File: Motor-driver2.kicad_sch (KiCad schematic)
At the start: 32 parts, among them J12 PINHD_1x4_Male, J15 PINHD_1x4_Male, U4 DRV8825PWP, U5 DRV8825PWP

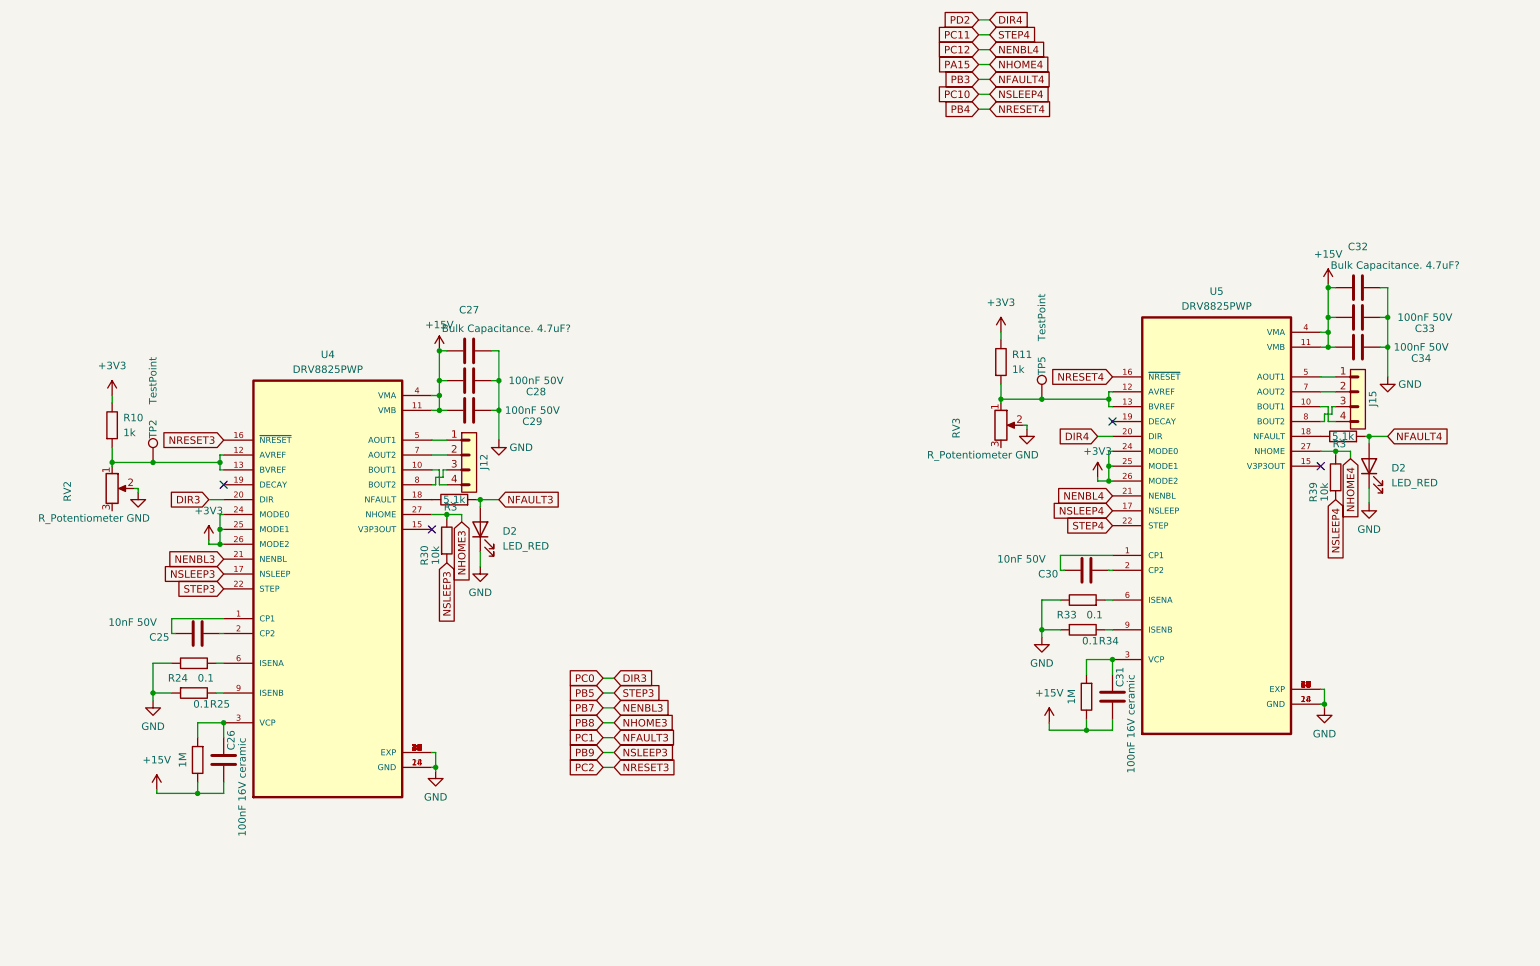
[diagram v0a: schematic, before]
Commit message: completly reroutet EVERYTHING
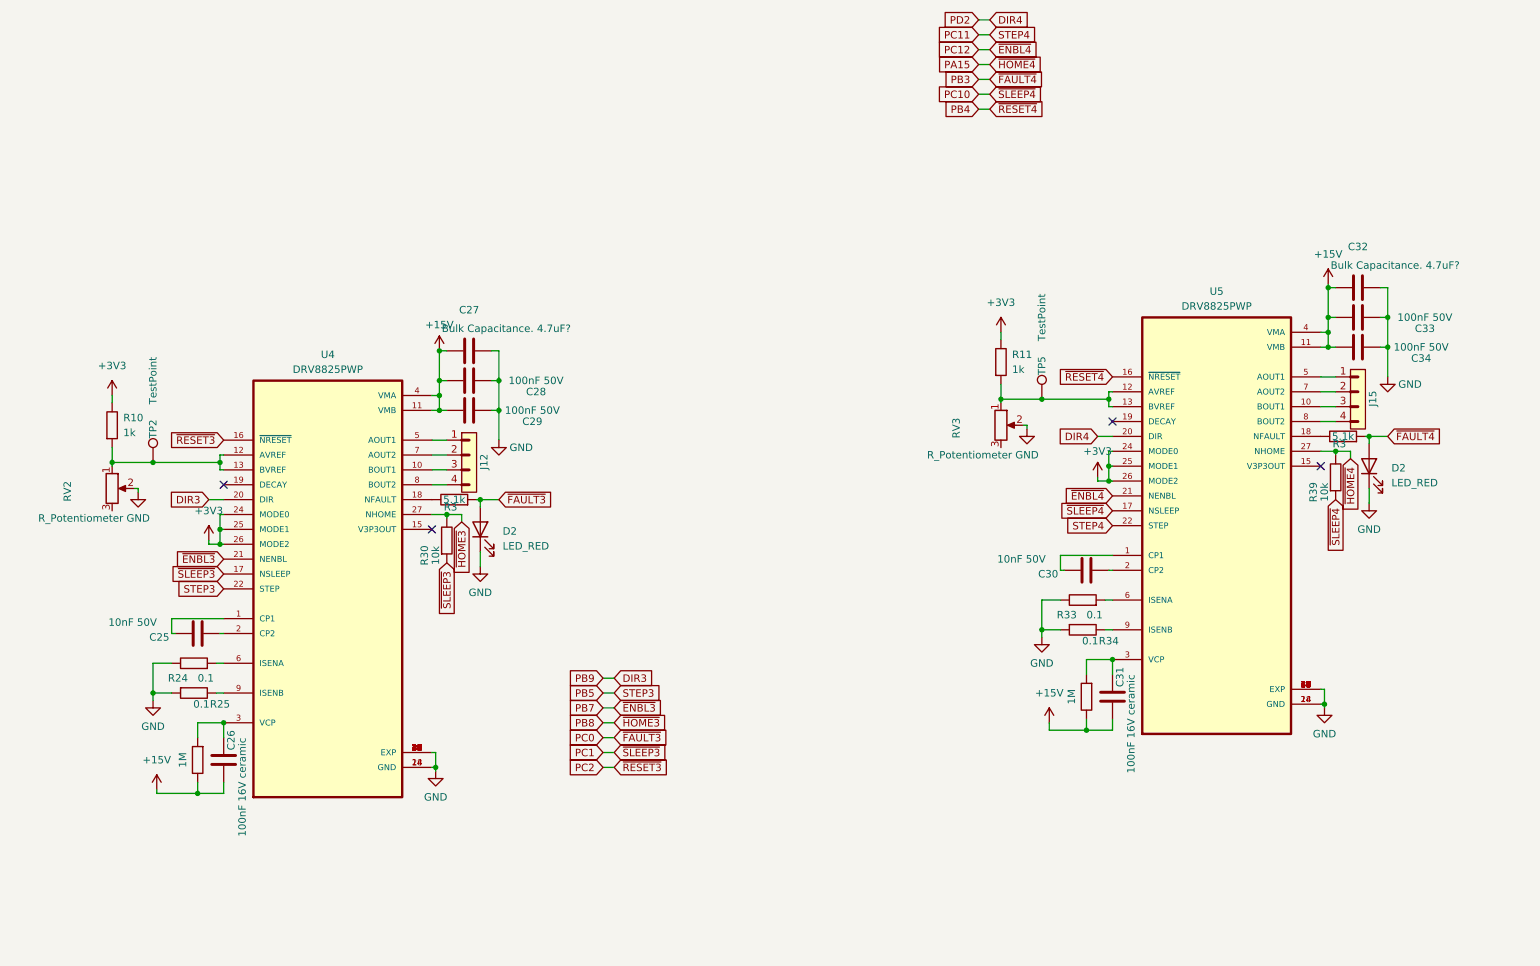
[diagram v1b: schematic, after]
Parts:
- RV2, RV3: footprint Potentiometer_THT:Potentiometer_ACP_CA6-H2,5_Horizontal -> poti:3386P1473LF
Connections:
- net at J15.3: now also U5.10 (BOUT1); no longer U5.8 (BOUT2)
- net at J15.4: now also U5.8 (BOUT2); no longer U5.10 (BOUT1)
- net at U4.10 (BOUT1): now also J12.3; no longer J12.4
- net at U4.8 (BOUT2): now also J12.4; no longer J12.3
- net NENBL3 renamed PB7
- net NENBL4 renamed PC12
- net NFAULT3 renamed PC0
- net NFAULT4 renamed PB3
- net NHOME3 renamed PB8
- net NHOME4 renamed PA15
- net NRESET3 renamed PC2
- net NRESET4 renamed PB4
- net NSLEEP3 renamed PC1
- net NSLEEP4 renamed PC10

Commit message: deTommaso approved version
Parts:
- removed C27, C32: Bulk Capacitance. 4.7uF?, Capacitor_SMD:C_0805_2012Metric, symbol Device:C
- removed TP2, TP5: TestPoint, TestPoint:TestPoint_Pad_D1.5mm, symbol Connector:TestPoint
- added C22 (x2): 10uF, Capacitor_THT:C_Radial_D5.0mm_H5.0mm_P2.00mm, symbol Device:C
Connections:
- net +15V: now also C22.2, C22.2
- net GND: now also C22.1, C22.1
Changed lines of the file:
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@@
   (junction (at 51.435 102.235) (diameter 0) (color 0 0 0 0)
   )
-  (junction (at 40.005 102.235) (diameter 0) (color 0 0 0 0)
-  )
   (junction (at 52.07 146.685) (diameter 0) (color 0 0 0 0)
   )
@@
   )
   (junction (at 184.785 91.44) (diameter 0) (color 0 0 0 0)
-  )
-  (junction (at 191.77 91.44) (diameter 0) (color 0 0 0 0)
   )
   (junction (at 199.39 147.955) (diameter 0) (color 0 0 0 0)
@@
     (stroke (width 0) (type default))
   )
-  (wire (pts (xy 33.02 102.235) (xy 40.005 102.235))
+  (wire (pts (xy 33.02 102.235) (xy 51.435 102.235))
     (stroke (width 0) (type default))
   )
@@
     (stroke (width 0) (type default))
   )
-  (wire (pts (xy 191.77 91.44) (xy 203.2 91.44))
+  (wire (pts (xy 184.785 91.44) (xy 203.2 91.44))
     (stroke (width 0) (type default))
   )
@@
     (stroke (width 0) (type default))
   )
-  (wire (pts (xy 40.005 102.235) (xy 51.435 102.235))
-    (stroke (width 0) (type default))
-  )
   (wire (pts (xy 116.84 144.145) (xy 118.745 144.145))
     (stroke (width 0) (type default))
@@
   )
   (wire (pts (xy 199.39 147.955) (xy 203.835 147.955))
-    (stroke (width 0) (type default))
-  )
-  (wire (pts (xy 184.785 91.44) (xy 191.77 91.44))
     (stroke (width 0) (type default))
   )
@@
     )
   )
-  (symbol (lib_id "Device:C") (at 93.98 83.185 270) (unit 1)
-    (in_bom yes) (on_board yes) (dnp no)
-    (property "Reference" "C27" (at 93.98 76.2 90)
-      (effects (font (size 1.27 1.27)))
-    )
-    (property "Value" "Bulk Capacitance. 4.7uF?" (at 100.33 79.375 90)
-      (effects (font (size 1.27 1.27)))
-    )
-    (property "Footprint" "Capacitor_SMD:C_0805_2012Metric" (at 90.17 84.1502 0)
-      (effects (font (size 1.27 1.27)) hide)
-    )
-    (property "Datasheet" "~" (at 93.98 83.185 0)
-      (effects (font (size 1.27 1.27)) hide)
-    )
-    (pin "1")
-    (pin "2")
-    (instances
-      (project "Doodle Drive"
-        (path "/3ec634aa-8c09-482d-9325-2288a4dbd68b/4a4951fa-be57-4d48-97a5-6be750b353b5"
-          (reference "C27") (unit 1)
+  (symbol (lib_id "Device:C") (at 245.745 72.39 270) (unit 1)
+    (in_bom yes) (on_board yes) (dnp no)
+    (property "Reference" "C22" (at 245.745 65.405 90)
+      (effects (font (size 1.27 1.27)))
+    )
+    (property "Value" "10uF" (at 246.38 68.58 90)
+      (effects (font (size 1.27 1.27)))
+    )
+    (property "Footprint" "Capacitor_THT:C_Radial_D5.0mm_H5.0mm_P2.00mm" (at 241.935 73.3552 0)
+      (effects (font (size 1.27 1.27)) hide)
+    )
+    (property "Datasheet" "~" (at 245.745 72.39 0)
+      (effects (font (size 1.27 1.27)) hide)
+    )
+    (pin "1")
+    (pin "2")
+    (instances
+      (project "Doodle Drive"
+        (path "/3ec634aa-8c09-482d-9325-2288a4dbd68b/ce40ab82-c304-4dd2-80f5-b6df1964b151"
+          (reference "C22") (unit 1)
+        )
+        (path "/3ec634aa-8c09-482d-9325-2288a4dbd68b/bef0954e-6024-4756-b9a6-5ea2a0825f13"
+          (reference "C37") (unit 1)
+        )
+        (path "/3ec634aa-8c09-482d-9325-2288a4dbd68b/4a4951fa-be57-4d48-97a5-6be750b353b5"
+          (reference "C32") (unit 1)
         )
       )
@@
   )
   (symbol (lib_id "power:+15V") (at 88.9 83.185 0) (unit 1)
-    (in_bom yes) (on_board yes) (dnp no) (fields_autoplaced)
+    (in_bom yes) (on_board yes) (dnp no)
     (property "Reference" "#PWR066" (at 88.9 86.995 0)
       (effects (font (size 1.27 1.27)) hide)
     )
-    (property "Value" "+15V" (at 88.9 78.74 0)
+    (property "Value" "+15V" (at 85.09 81.28 0)
       (effects (font (size 1.27 1.27)))
     )
@@
         (path "/3ec634aa-8c09-482d-9325-2288a4dbd68b/4a4951fa-be57-4d48-97a5-6be750b353b5"
           (reference "#PWR054") (unit 1)
-        )
-      )
-    )
-  )
-  (symbol (lib_id "Connector:TestPoint") (at 40.005 102.235 0) (unit 1)
-    (in_bom yes) (on_board yes) (dnp no)
-    (property "Reference" "TP2" (at 40.005 96.52 90)
-      (effects (font (size 1.27 1.27)))
-    )
-    (property "Value" "TestPoint" (at 40.005 88.265 90)
-      (effects (font (size 1.27 1.27)))
-    )
-    (property "Footprint" "TestPoint:TestPoint_Pad_D1.5mm" (at 45.085 102.235 0)
-      (effects (font (size 1.27 1.27)) hide)
-    )
-    (property "Datasheet" "~" (at 45.085 102.235 0)
-      (effects (font (size 1.27 1.27)) hide)
-    )
-    (pin "1")
-    (instances
-      (project "Doodle Drive"
-        (path "/3ec634aa-8c09-482d-9325-2288a4dbd68b/4a4951fa-be57-4d48-97a5-6be750b353b5"
-          (reference "TP2") (unit 1)
-        )
-        (path "/3ec634aa-8c09-482d-9325-2288a4dbd68b/ce40ab82-c304-4dd2-80f5-b6df1964b151"
-          (reference "TP42") (unit 1)
         )
       )
@@
     )
   )
-  (symbol (lib_id "Device:C") (at 245.745 72.39 270) (unit 1)
-    (in_bom yes) (on_board yes) (dnp no)
-    (property "Reference" "C32" (at 245.745 65.405 90)
-      (effects (font (size 1.27 1.27)))
-    )
-    (property "Value" "Bulk Capacitance. 4.7uF?" (at 252.095 68.58 90)
-      (effects (font (size 1.27 1.27)))
-    )
-    (property "Footprint" "Capacitor_SMD:C_0805_2012Metric" (at 241.935 73.3552 0)
-      (effects (font (size 1.27 1.27)) hide)
-    )
-    (property "Datasheet" "~" (at 245.745 72.39 0)
-      (effects (font (size 1.27 1.27)) hide)
-    )
-    (pin "1")
-    (pin "2")
-    (instances
-      (project "Doodle Drive"
-        (path "/3ec634aa-8c09-482d-9325-2288a4dbd68b/4a4951fa-be57-4d48-97a5-6be750b353b5"
-          (reference "C32") (unit 1)
-        )
-      )
-    )
-  )
   (symbol (lib_id "power:+3V3") (at 49.53 115.57 0) (unit 1)
     (in_bom yes) (on_board yes) (dnp no) (fields_autoplaced)
@@
         (path "/3ec634aa-8c09-482d-9325-2288a4dbd68b/4a4951fa-be57-4d48-97a5-6be750b353b5"
           (reference "C31") (unit 1)
-        )
-      )
-    )
-  )
-  (symbol (lib_id "Connector:TestPoint") (at 191.77 91.44 0) (unit 1)
-    (in_bom yes) (on_board yes) (dnp no)
-    (property "Reference" "TP5" (at 191.77 85.725 90)
-      (effects (font (size 1.27 1.27)))
-    )
-    (property "Value" "TestPoint" (at 191.77 77.47 90)
-      (effects (font (size 1.27 1.27)))
-    )
-    (property "Footprint" "TestPoint:TestPoint_Pad_D1.5mm" (at 196.85 91.44 0)
-      (effects (font (size 1.27 1.27)) hide)
-    )
-    (property "Datasheet" "~" (at 196.85 91.44 0)
-      (effects (font (size 1.27 1.27)) hide)
-    )
-    (pin "1")
-    (instances
-      (project "Doodle Drive"
-        (path "/3ec634aa-8c09-482d-9325-2288a4dbd68b/4a4951fa-be57-4d48-97a5-6be750b353b5"
-          (reference "TP5") (unit 1)
-        )
-        (path "/3ec634aa-8c09-482d-9325-2288a4dbd68b/ce40ab82-c304-4dd2-80f5-b6df1964b151"
-          (reference "TP42") (unit 1)
         )
       )
@@
         )
       )
+    )
+  )
+  (symbol (lib_id "Device:C") (at 93.98 83.185 270) (unit 1)
+    (in_bom yes) (on_board yes) (dnp no)
+    (property "Reference" "C22" (at 93.98 76.2 90)
+      (effects (font (size 1.27 1.27)))
+    )
+    (property "Value" "10uF" (at 94.615 79.375 90)
+      (effects (font (size 1.27 1.27)))
+    )
+    (property "Footprint" "Capacitor_THT:C_Radial_D5.0mm_H5.0mm_P2.00mm" (at 90.17 84.1502 0)
+      (effects (font (size 1.27 1.27)) hide)
+    )
+    (property "Datasheet" "~" (at 93.98 83.185 0)
+      (effects (font (size 1.27 1.27)) hide)
+    )
+    (pin "1")
+    (pin "2")
+    (instances
+      (project "Doodle Drive"
+        (path "/3ec634aa-8c09-482d-9325-2288a4dbd68b/ce40ab82-c304-4dd2-80f5-b6df1964b151"
+          (reference "C22") (unit 1)
+        )
+        (path "/3ec634aa-8c09-482d-9325-2288a4dbd68b/bef0954e-6024-4756-b9a6-5ea2a0825f13"
+          (reference "C37") (unit 1)
+        )
+        (path "/3ec634aa-8c09-482d-9325-2288a4dbd68b/4a4951fa-be57-4d48-97a5-6be750b353b5"
+          (reference "C27") (unit 1)
+        )
+      )

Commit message: bestellte version
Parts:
- C25, C30: value 10nF 50V -> 10nF
- C26, C31: value 100nF 16V ceramic -> 100nF
- C28, C29, C33, C34: value 100nF 50V -> 100nF
- R24, R25, R33, R34: footprint Resistor_SMD:R_0805_2012Metric -> Resistor_SMD:R_1206_3216Metric
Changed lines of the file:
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@@
       (effects (font (size 1.27 1.27)) (justify left))
     )
-    (property "Value" "10nF 50V" (at 184.15 118.745 90)
+    (property "Value" "10nF" (at 184.15 118.745 90)
       (effects (font (size 1.27 1.27)) (justify left))
     )
@@
       (effects (font (size 1.27 1.27)))
     )
-    (property "Value" "100nF 50V" (at 256.54 82.55 90)
+    (property "Value" "100nF" (at 256.54 82.55 90)
       (effects (font (size 1.27 1.27)))
     )
@@
       (effects (font (size 1.27 1.27)))
     )
-    (property "Value" "100nF 50V" (at 105.41 88.265 90)
+    (property "Value" "100nF" (at 105.41 88.265 90)
       (effects (font (size 1.27 1.27)))
     )
@@
       (effects (font (size 1.27 1.27)) (justify right))
     )
-    (property "Footprint" "Resistor_SMD:R_0805_2012Metric" (at 197.866 121.412 0)
+    (property "Footprint" "Resistor_SMD:R_1206_3216Metric" (at 197.866 121.412 0)
       (effects (font (size 1.27 1.27)) hide)
     )
@@
       (effects (font (size 1.27 1.27)) (justify left))
     )
-    (property "Value" "10nF 50V" (at 32.385 129.54 90)
+    (property "Value" "10nF" (at 32.385 129.54 90)
       (effects (font (size 1.27 1.27)) (justify left))
     )
@@
       (effects (font (size 1.27 1.27)) (justify left))
     )
-    (property "Value" "100nF 16V ceramic" (at 55.245 149.225 90)
+    (property "Value" "100nF" (at 55.245 149.225 90)
       (effects (font (size 1.27 1.27)) (justify left))
     )
@@
       (effects (font (size 1.27 1.27)))
     )
-    (property "Value" "100nF 50V" (at 104.775 93.345 90)
+    (property "Value" "100nF" (at 104.775 93.345 90)
       (effects (font (size 1.27 1.27)))
     )
@@
       (effects (font (size 1.27 1.27)) (justify right))
     )
-    (property "Footprint" "Resistor_SMD:R_0805_2012Metric" (at 46.101 132.207 0)
+    (property "Footprint" "Resistor_SMD:R_1206_3216Metric" (at 46.101 132.207 0)
       (effects (font (size 1.27 1.27)) hide)
     )
@@
       (effects (font (size 1.27 1.27)))
     )
-    (property "Footprint" "Resistor_SMD:R_0805_2012Metric" (at 199.644 135.128 0)
+    (property "Footprint" "Resistor_SMD:R_1206_3216Metric" (at 199.644 135.128 0)
       (effects (font (size 1.27 1.27)) hide)
     )
@@
       (effects (font (size 1.27 1.27)) (justify left))
     )
-    (property "Value" "100nF 16V ceramic" (at 207.01 138.43 90)
+    (property "Value" "100nF" (at 207.01 138.43 90)
       (effects (font (size 1.27 1.27)) (justify left))
     )
@@
       (effects (font (size 1.27 1.27)))
     )
-    (property "Footprint" "Resistor_SMD:R_0805_2012Metric" (at 47.879 145.923 0)
+    (property "Footprint" "Resistor_SMD:R_1206_3216Metric" (at 47.879 145.923 0)
       (effects (font (size 1.27 1.27)) hide)
     )
@@
       (effects (font (size 1.27 1.27)))
     )
-    (property "Value" "100nF 50V" (at 257.175 77.47 90)
-      (effects (font (size 1.27 1.27)))
-    )
+    (property "Value" "100nF" (at 257.175 77.47 90)
+      (effects (font (size 1.27 1.27)))
+    )
